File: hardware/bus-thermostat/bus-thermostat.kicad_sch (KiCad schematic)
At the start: 2 parts

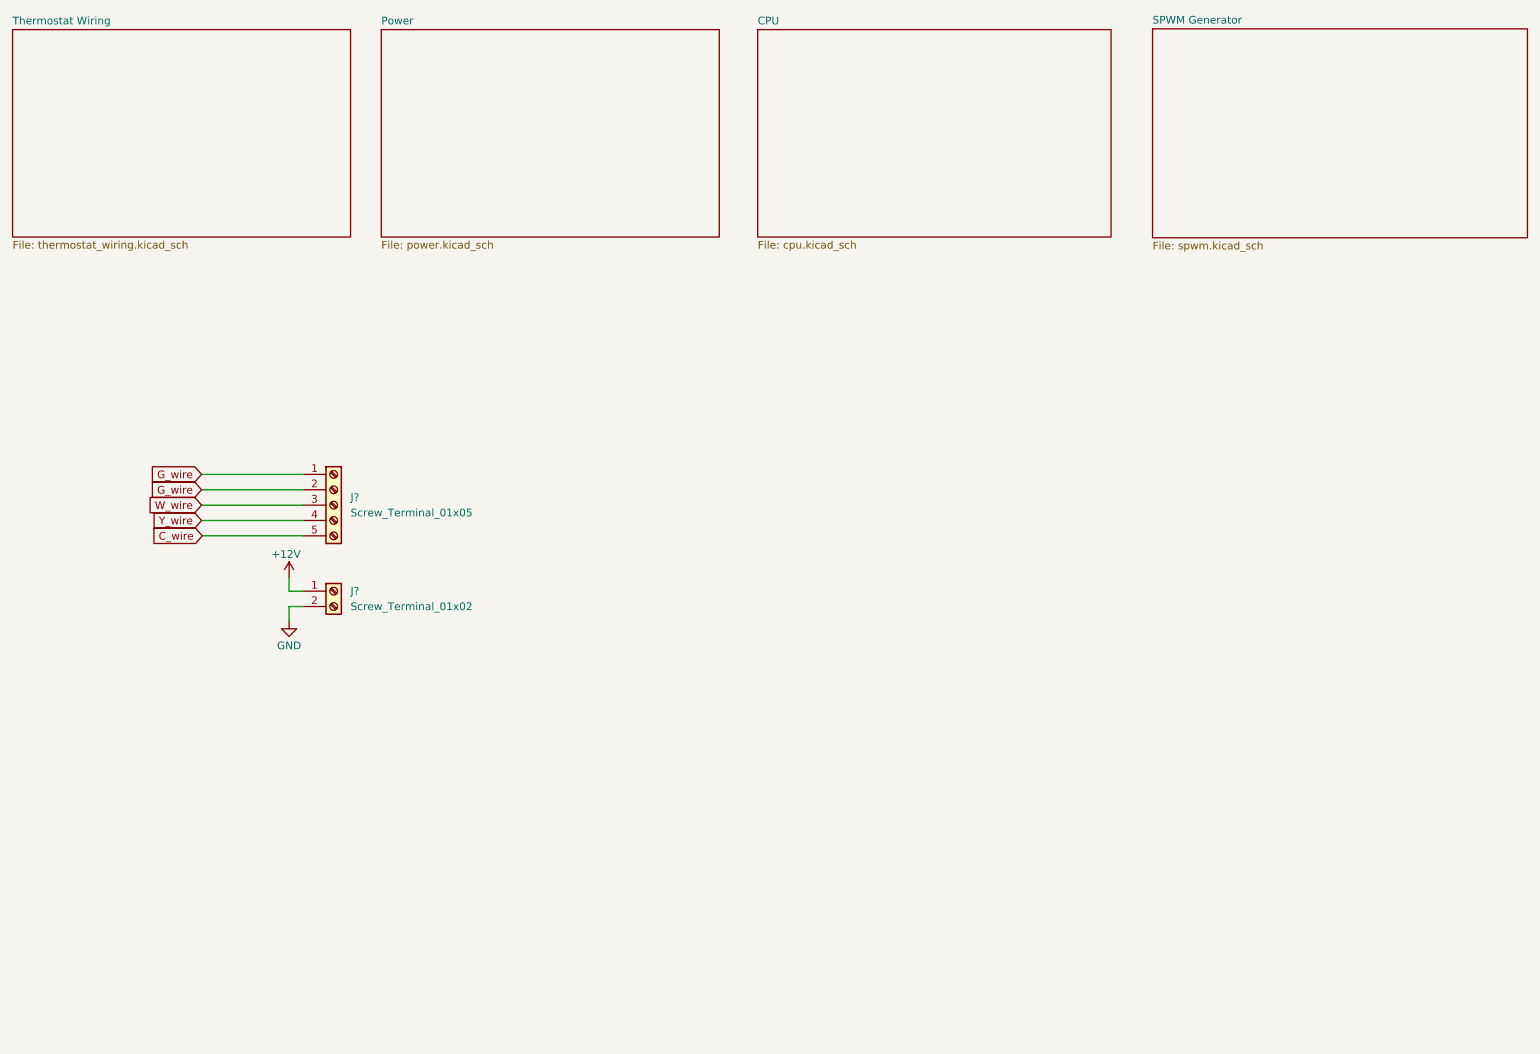
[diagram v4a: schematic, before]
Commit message: Rework the AC path generation again. Opamps only.
- awaiting the completion of analog circuit analysis
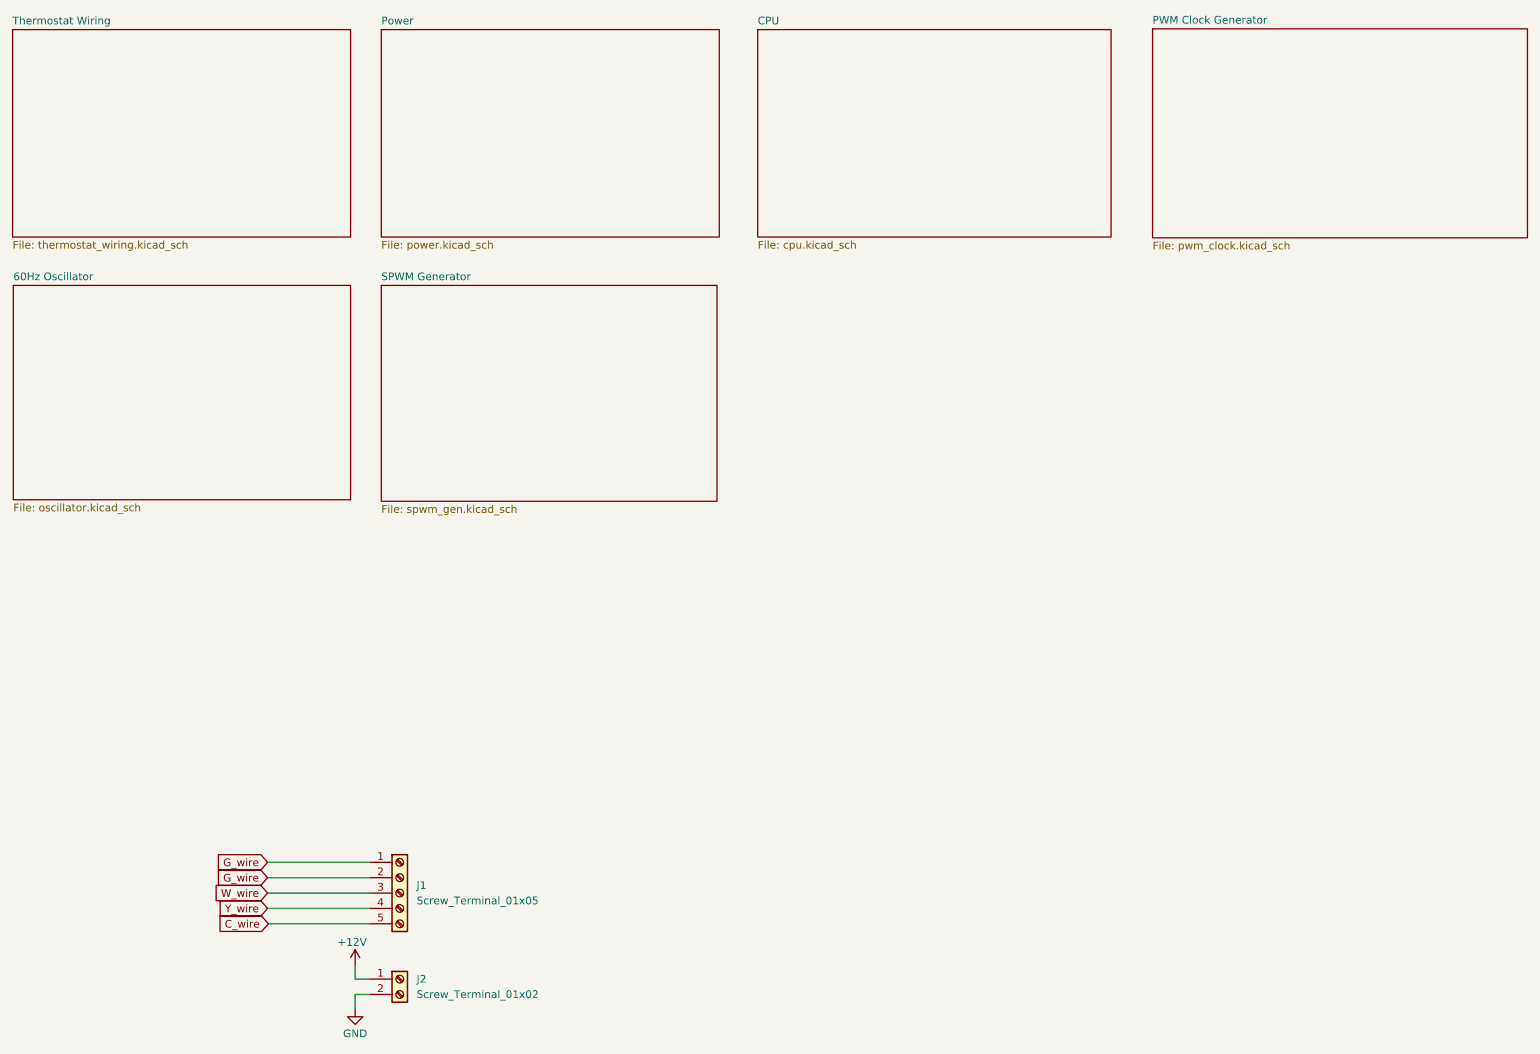
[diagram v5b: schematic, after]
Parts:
- gave numbers to parts that had none: 2
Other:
- added sheet 60Hz Oscillator (oscillator.kicad_sch)
- added sheet PWM Clock Generator (pwm_clock.kicad_sch)
- sheet SPWM Generator: file spwm.kicad_sch -> spwm_gen.kicad_sch
- moved on the sheet: J1, J2

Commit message: Update some components
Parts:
- J2: footprint (none) -> TerminalBlock_TE-Connectivity:TerminalBlock_TE_282834-2_1x02_P2.54mm_Horizontal
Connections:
- net +12V renamed +BATT
